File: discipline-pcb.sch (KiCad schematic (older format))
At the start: 164 parts, among them J1 AVR-ISP-6, SW1 KEYSW, SW10 KEYSW, SW11 KEYSW, SW12 KEYSW, SW13 KEYSW, SW14 KEYSW, SW15 KEYSW, SW16 KEYSW, SW17 KEYSW, SW18 KEYSW, SW19 KEYSW, SW2 KEYSW, SW20 KEYSW, SW21 KEYSW, SW22 KEYSW, SW23 KEYSW, SW24 KEYSW, SW25 KEYSW, SW26 KEYSW, SW27 KEYSW, SW28 KEYSW, SW29 KEYSW, SW3 KEYSW, SW30 KEYSW, SW31 KEYSW, SW32 KEYSW, SW33 KEYSW, SW34 KEYSW, SW35 KEYSW, SW36 KEYSW, SW37 KEYSW, SW38 KEYSW, SW39 KEYSW, SW4 KEYSW, SW40 KEYSW, SW41 KEYSW, SW42 KEYSW, SW43 KEYSW, SW44 KEYSW, SW45 KEYSW, SW46 KEYSW, SW47 KEYSW, SW48 KEYSW, SW49 KEYSW, SW5 KEYSW, SW50 KEYSW, SW51 KEYSW, SW52 KEYSW, SW53 KEYSW, SW54 KEYSW, SW55 KEYSW, SW56 KEYSW, SW57 KEYSW, SW58 KEYSW, SW59 KEYSW, SW6 KEYSW, SW60 KEYSW, SW61 KEYSW, SW62 KEYSW, SW63 KEYSW, SW64 KEYSW, SW65 KEYSW, SW66 KEYSW, SW67 KEYSW, SW68 KEYSW, SW69 KEYSW, SW7 KEYSW, SW70 KEYSW, SW71 KEYSW, SW72 KEYSW, SW73 KEYSW, SW74 KEYSW, SW8 KEYSW, SW9 KEYSW, U1 ATmega32A-PU, Y1 Crystal

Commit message: hopefully made it ISO compatible
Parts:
- added D75: (no value), cftkb:D_DO-35_SOD27_P5.08mm_Horizontal, symbol Device:D
- added SW75, SWb43: KEYSW, cftkb:SW_Cherry_MX1A_1.00u_PCB-NOSCREEN, symbol discipline-pcb-rescue:KEYSW-keyboard_parts
- added SWb29: KEYSW, MX_Only:MXOnly-ISO-ROTATED-ReversedStabilizers-NoLED, symbol discipline-pcb-rescue:KEYSW-keyboard_parts
- added SWb45: KEYSW, cftkb:SW_Cherry_MX1A_1.25u_PCBNOSCREEN, symbol discipline-pcb-rescue:KEYSW-keyboard_parts
- BOOT1, RESET1: symbol keyboard_parts:SW_PUSH -> discipline-pcb-rescue:SW_PUSH-keyboard_parts
- SW1, SW10, SW11, SW12, SW13, SW14, SW15, SW16, SW17, SW18, SW19, SW2, SW20, SW21, SW22, SW23, SW24, SW25, SW26, SW27, SW28, SW29, SW3, SW30, SW31, SW32, SW33, SW34, SW35, SW36, SW37, SW38, SW39, SW4, SW40, SW41, SW42, SW43, SW44, SW45, SW46, SW47, SW48, SW49, SW5, SW50, SW51, SW52, SW53, SW54, SW55, SW56, SW57, SW58, SW59, SW6, SW60, SW61, SW62, SW63, SW64, SW65, SW66, SW67, SW68, SW69, SW7, SW70, SW71, SW72, SW73, SW74, SW8, SW9: symbol keyboard_parts:KEYSW -> discipline-pcb-rescue:KEYSW-keyboard_parts
- USB1: symbol Type-C:USB_C_GCT_USB4085 -> discipline-pcb-rescue:USB_C_GCT_USB4085-Type-C
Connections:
- wire segments 342 -> 352

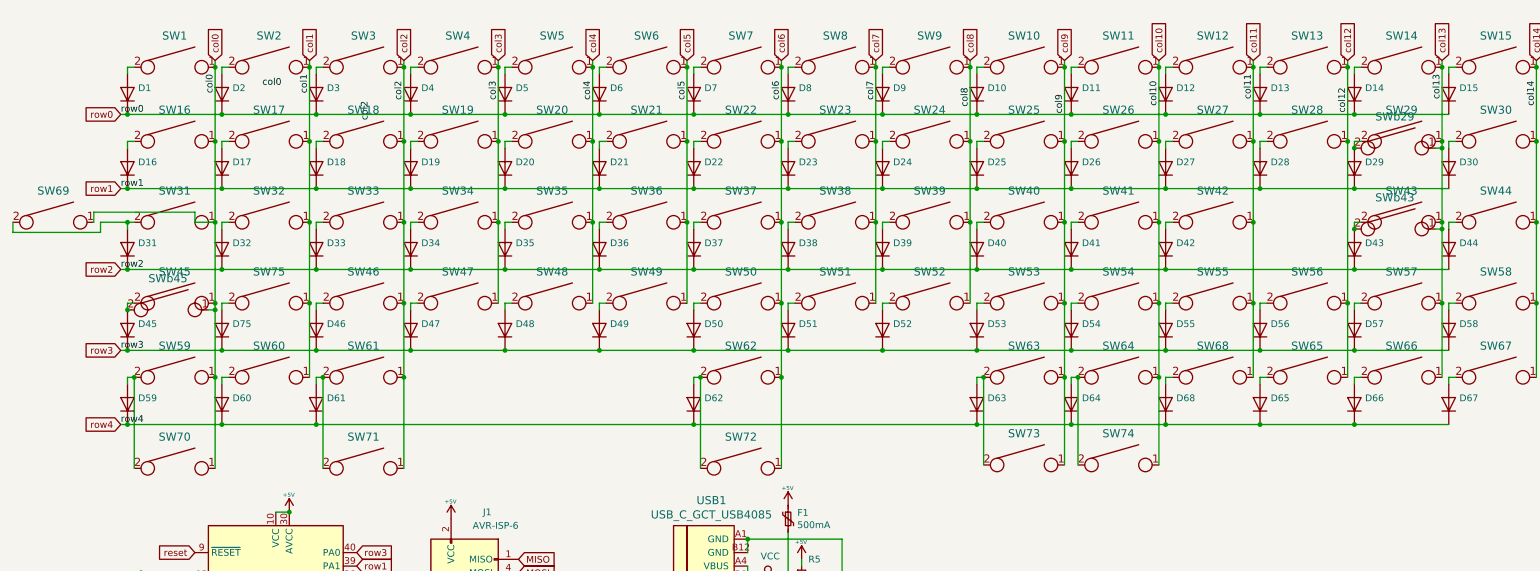
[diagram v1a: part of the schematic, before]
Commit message: fixed some footprints and removed switch options
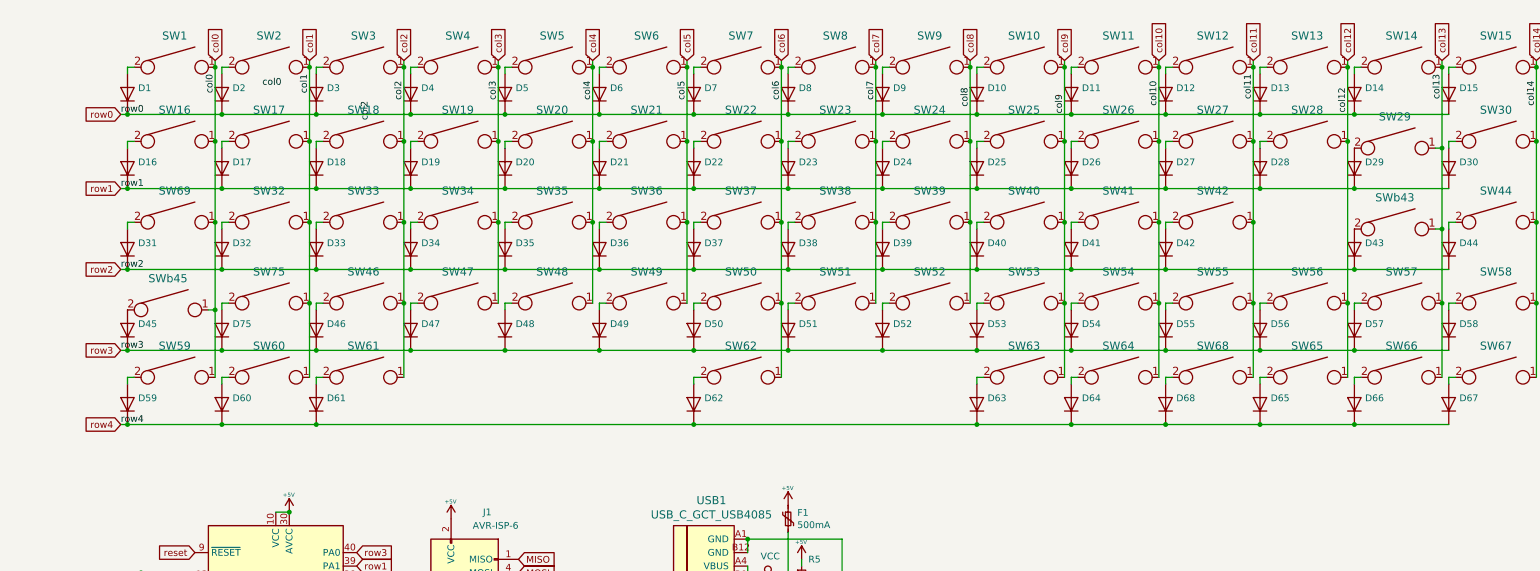
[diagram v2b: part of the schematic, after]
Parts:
- removed SW31: KEYSW, cftkb:SW_Cherry_MX1A_1.75u_PCBNOSCREEN, symbol discipline-pcb-rescue:KEYSW-keyboard_parts
- removed SW43, SW45: KEYSW, cftkb:SW_Cherry_MX1A_2.25u_PCBNOSCREEN, symbol discipline-pcb-rescue:KEYSW-keyboard_parts
- removed SW70, SW71, SW73, SW74: KEYSW, cftkb:SW_Cherry_MX1A_1.50u_PCBNOSCREEN, symbol discipline-pcb-rescue:KEYSW-keyboard_parts
- removed SW72: KEYSW, cftkb:SW_Cherry_MX1A_1.00u_PCB-NOSCREEN, symbol discipline-pcb-rescue:KEYSW-keyboard_parts
- removed SWb29: KEYSW, MX_Only:MXOnly-ISO-ROTATED-ReversedStabilizers-NoLED, symbol discipline-pcb-rescue:KEYSW-keyboard_parts
- C1, C2: footprint cftkb:D_DO-35_SOD27_P5.08mm_Horizontal -> Capacitor_THT:C_Disc_D3.4mm_W2.1mm_P2.50mm
- C3: footprint cftkb:D_DO-35_SOD27_P5.08mm_Horizontal -> Capacitor_THT:CP_Radial_D4.0mm_P1.50mm
- C4, C5: footprint cftkb:D_DO-35_SOD27_P5.08mm_Horizontal -> Capacitor_THT:C_Disc_D5.0mm_W2.5mm_P5.00mm
- SW29: footprint cftkb:SW_Cherry_MX1A_1.50u_PCBNOSCREEN -> cftkb:SW_Cherry_MX1A_2.00u_PCBNOSCREEN
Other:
- moved on the sheet: SW69
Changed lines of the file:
@@
 	11300 3500 11300 3550
-$Comp
-L discipline-pcb-rescue:KEYSW-keyboard_parts SW29
-U 1 1 5BDD4B49
-P 12350 3500
-F 0 "SW29" H 12350 3733 60  0000 C CNN
-F 1 "KEYSW" H 12350 3400 60  0001 C CNN
-F 2 "cftkb:SW_Cherry_MX1A_1.50u_PCBNOSCREEN" H 12350 3500 60  0001 C CNN
-F 3 "" H 12350 3500 60  0000 C CNN
-	1    12350 3500
-	1    0    0    -1
-$EndComp
 $Comp
 L Device:D D29
@@
 	0    -1   -1   0
 $EndComp
-Wire Wire Line
-	12050 3500 12000 3500
-Wire Wire Line
-	12000 3500 12000 3550
 $Comp
 L discipline-pcb-rescue:KEYSW-keyboard_parts SW30
@@
 	12700 3500 12700 3550
 $Comp
-L discipline-pcb-rescue:KEYSW-keyboard_parts SW31
-U 1 1 5BE2E393
-P 3250 4100
-F 0 "SW31" H 3250 4333 60  0000 C CNN
-F 1 "KEYSW" H 3250 4000 60  0001 C CNN
-F 2 "cftkb:SW_Cherry_MX1A_1.75u_PCBNOSCREEN" H 3250 4100 60  0001 C CNN
-F 3 "" H 3250 4100 60  0000 C CNN
-	1    3250 4100
-	1    0    0    -1
-$EndComp
-$Comp
 L Device:D D31
 U 1 1 5BE2E39A
@@
 	0    -1   -1   0
 $EndComp
-Wire Wire Line
-	2950 4100 2900 4100
-Wire Wire Line
-	2900 4100 2900 4150
 $Comp
 L discipline-pcb-rescue:KEYSW-keyboard_parts SW32
@@
 	10600 4100 10600 4150
 $Comp
-L discipline-pcb-rescue:KEYSW-keyboard_parts SW43
-U 1 1 5BE2E453
-P 12350 4100
-F 0 "SW43" H 12350 4333 60  0000 C CNN
-F 1 "KEYSW" H 12350 4000 60  0001 C CNN
-F 2 "cftkb:SW_Cherry_MX1A_2.25u_PCBNOSCREEN" H 12350 4100 60  0001 C CNN
-F 3 "" H 12350 4100 60  0000 C CNN
-	1    12350 4100
-	1    0    0    -1
-$EndComp
-$Comp
 L Device:D D43
 U 1 1 5BE2E45A
@@
 	0    -1   -1   0
 $EndComp
-Wire Wire Line
-	12050 4100 12000 4100
-Wire Wire Line
-	12000 4100 12000 4150
 $Comp
 L discipline-pcb-rescue:KEYSW-keyboard_parts SW44
@@
 	12700 4100 12700 4150
 $Comp
-L discipline-pcb-rescue:KEYSW-keyboard_parts SW45
-U 1 1 5BE34833
-P 3250 4700
-F 0 "SW45" H 3250 4933 60  0000 C CNN
-F 1 "KEYSW" H 3250 4600 60  0001 C CNN
-F 2 "cftkb:SW_Cherry_MX1A_2.25u_PCBNOSCREEN" H 3250 4700 60  0001 C CNN
-F 3 "" H 3250 4700 60  0000 C CNN
-	1    3250 4700
-	1    0    0    -1
-$EndComp
-$Comp
 L Device:D D45
 U 1 1 5BE3483A
@@
 	0    -1   -1   0
 $EndComp
-Wire Wire Line
-	2950 4700 2900 4700
-Wire Wire Line
-	2900 4700 2900 4750
 $Comp
 L discipline-pcb-rescue:KEYSW-keyboard_parts SW46
@@
 F 0 "C2" H 3100 7300 50  0000 L CNN
 F 1 "22p" H 3100 7200 50  0000 L CNN
-F 2 "cftkb:D_DO-35_SOD27_P5.08mm_Horizontal" H 3000 7200 50  0001 C CNN
+F 2 "Capacitor_THT:C_Disc_D3.4mm_W2.1mm_P2.50mm" H 3000 7200 50  0001 C CNN
 F 3 "~" H 3000 7200 50  0001 C CNN
 	1    3000 7200
@@
 F 0 "C1" H 2650 7300 50  0000 L CNN
 F 1 "22p" H 2600 7200 50  0000 L CNN
-F 2 "cftkb:D_DO-35_SOD27_P5.08mm_Horizontal" H 2850 7200 50  0001 C CNN
+F 2 "Capacitor_THT:C_Disc_D3.4mm_W2.1mm_P2.50mm" H 2850 7200 50  0001 C CNN
 F 3 "~" H 2850 7200 50  0001 C CNN
 	1    2850 7200
@@
 F 0 "C3" H 5350 10250 50  0000 L CNN
 F 1 "4.7u" H 5300 9950 50  0000 L CNN
-F 2 "cftkb:D_DO-35_SOD27_P5.08mm_Horizontal" H 5400 10100 50  0001 C CNN
+F 2 "Capacitor_THT:CP_Radial_D4.0mm_P1.50mm" H 5400 10100 50  0001 C CNN
 F 3 "~" H 5400 10100 50  0001 C CNN
 	1    5400 10100
@@
 F 0 "C4" H 5500 10250 50  0000 L CNN
 F 1 "0.1u" H 5500 9950 50  0000 L CNN
-F 2 "cftkb:D_DO-35_SOD27_P5.08mm_Horizontal" H 5550 10100 50  0001 C CNN
+F 2 "Capacitor_THT:C_Disc_D5.0mm_W2.5mm_P5.00mm" H 5550 10100 50  0001 C CNN
 F 3 "~" H 5550 10100 50  0001 C CNN
 	1    5550 10100
@@
 F 0 "C5" H 5650 10250 50  0000 L CNN
 F 1 "0.1u" H 5700 9950 50  0000 L CNN
-F 2 "cftkb:D_DO-35_SOD27_P5.08mm_Horizontal" H 5700 10100 50  0001 C CNN
+F 2 "Capacitor_THT:C_Disc_D5.0mm_W2.5mm_P5.00mm" H 5700 10100 50  0001 C CNN
 F 3 "~" H 5700 10100 50  0001 C CNN
 	1    5700 10100
@@
 Connection ~ 3550 3500
 Wire Wire Line
-	3550 3500 3550 4100
-Connection ~ 3550 4100
-Wire Wire Line
-	3550 4100 3550 4700
-Connection ~ 3550 4700
-Wire Wire Line
-	3550 4700 3550 4750
-Wire Wire Line
 	4250 2900 4250 2950
 Connection ~ 4250 2950
@@
 	12650 2900 12650 2950
 Connection ~ 12650 2950
-Wire Wire Line
-	12650 2950 12650 3500
-Connection ~ 12650 3500
-Wire Wire Line
-	12650 3500 12650 3550
-Connection ~ 12650 4100
-Wire Wire Line
-	12650 4100 12650 4150
 Connection ~ 12650 4700
 Wire Wire Line
@@
 L discipline-pcb-rescue:KEYSW-keyboard_parts SW69
 U 1 1 5DC1DEA4
-P 2350 4100
-F 0 "SW69" H 2350 4333 60  0000 C CNN
-F 1 "KEYSW" H 2350 4000 60  0001 C CNN
-F 2 "cftkb:SW_Cherry_MX1A_1.25u_PCBNOSCREEN" H 2350 4100 60  0001 C CNN
-F 3 "" H 2350 4100 60  0000 C CNN
-	1    2350 4100
-	1    0    0    -1
-$EndComp
-Wire Wire Line
-	2650 4100 2650 4025
-Wire Wire Line
-	2650 4025 3400 4025
-Wire Wire Line
-	3400 4025 3400 4100
-Wire Wire Line
-	3400 4100 3550 4100
-Wire Wire Line
-	2900 4100 2700 4100
-Wire Wire Line
-	2700 4100 2700 4175
-Wire Wire Line
-	2700 4175 2050 4175
-Wire Wire Line
-	2050 4175 2050 4100
-Connection ~ 2900 4100
-$Comp
-L discipline-pcb-rescue:KEYSW-keyboard_parts SW70
-U 1 1 5DC5E2A2
-P 3250 5925
-F 0 "SW70" H 3250 6158 60  0000 C CNN
-F 1 "KEYSW" H 3250 5825 60  0001 C CNN
-F 2 "cftkb:SW_Cherry_MX1A_1.50u_PCBNOSCREEN" H 3250 5925 60  0001 C CNN
-F 3 "" H 3250 5925 60  0000 C CNN
-	1    3250 5925
-	1    0    0    -1
-$EndComp
-Wire Wire Line
-	2950 5925 2950 5250
-Connection ~ 2950 5250
-Wire Wire Line
-	3550 5925 3550 5250
-Connection ~ 3550 5250
-$Comp
-L discipline-pcb-rescue:KEYSW-keyboard_parts SW71
-U 1 1 5DC9EC8E
-P 4650 5925
-F 0 "SW71" H 4650 6158 60  0000 C CNN
-F 1 "KEYSW" H 4650 5825 60  0001 C CNN
-F 2 "cftkb:SW_Cherry_MX1A_1.50u_PCBNOSCREEN" H 4650 5925 60  0001 C CNN
-F 3 "" H 4650 5925 60  0000 C CNN
-	1    4650 5925
-	1    0    0    -1
-$EndComp
-Wire Wire Line
-	4350 5925 4350 5250
-Connection ~ 4350 5250
-Wire Wire Line
-	4950 5925 4950 5250
-Connection ~ 4950 5250
-$Comp
-L discipline-pcb-rescue:KEYSW-keyboard_parts SW72
-U 1 1 5DCE7558
-P 7450 5925
-F 0 "SW72" H 7450 6158 60  0000 C CNN
-F 1 "KEYSW" H 7450 5825 60  0001 C CNN
-F 2 "cftkb:SW_Cherry_MX1A_1.00u_PCB-NOSCREEN" H 7450 5925 60  0001 C CNN
-F 3 "" H 7450 5925 60  0000 C CNN
-	1    7450 5925
-	1    0    0    -1
-$EndComp
-Wire Wire Line
-	7150 5925 7150 5250
-Connection ~ 7150 5250
-Wire Wire Line
-	7750 5925 7750 5250
-Connection ~ 7750 5250
-$Comp
-L discipline-pcb-rescue:KEYSW-keyboard_parts SW73
-U 1 1 5DD3207D
-P 9550 5900
-F 0 "SW73" H 9550 6133 60  0000 C CNN
-F 1 "KEYSW" H 9550 5800 60  0001 C CNN
-F 2 "cftkb:SW_Cherry_MX1A_1.50u_PCBNOSCREEN" H 9550 5900 60  0001 C CNN
-F 3 "" H 9550 5900 60  0000 C CNN
-	1    9550 5900
-	1    0    0    -1
-$EndComp
-Wire Wire Line
-	9250 5900 9250 5250
-Connection ~ 9250 5250
-Wire Wire Line
-	9850 5900 9850 5250
-Connection ~ 9850 5250
-$Comp
-L discipline-pcb-rescue:KEYSW-keyboard_parts SW74
-U 1 1 5DD72960
-P 10250 5900
-F 0 "SW74" H 10250 6133 60  0000 C CNN
-F 1 "KEYSW" H 10250 5800 60  0001 C CNN
-F 2 "cftkb:SW_Cherry_MX1A_1.50u_PCBNOSCREEN" H 10250 5900 60  0001 C CNN
-F 3 "" H 10250 5900 60  0000 C CNN
-	1    10250 5900
-	1    0    0    -1
-$EndComp
-Wire Wire Line
-	9950 5900 9950 5250
-Connection ~ 9950 5250
-Wire Wire Line
-	10550 5900 10550 5250
-Connection ~ 10550 5250
+P 3250 4100
+F 0 "SW69" H 3250 4333 60  0000 C CNN
+F 1 "KEYSW" H 3250 4000 60  0001 C CNN
+F 2 "cftkb:SW_Cherry_MX1A_1.25u_PCBNOSCREEN" H 3250 4100 60  0001 C CNN
+F 3 "" H 3250 4100 60  0000 C CNN
+	1    3250 4100
+	1    0    0    -1
+$EndComp
 $Comp
 L MCU_Microchip_ATmega:ATmega32A-PU U1
@@
 $EndComp
 Connection ~ 4100 6250
-$Comp
-L discipline-pcb-rescue:KEYSW-keyboard_parts SWb29
-U 1 1 5DB34BFB
-P 12300 3550
-F 0 "SWb29" H 12300 3783 60  0000 C CNN
-F 1 "KEYSW" H 12300 3450 60  0001 C CNN
-F 2 "MX_Only:MXOnly-ISO-ROTATED-ReversedStabilizers-NoLED" H 12300 3550 60  0001 C CNN
-F 3 "" H 12300 3550 60  0000 C CNN
-	1    12300 3550
-	1    0    0    -1
-$EndComp
-Connection ~ 12000 3550
 Wire Wire Line
 	12600 3550 12650 3550
 Connection ~ 12650 3550
-Wire Wire Line
-	12650 3550 12650 4100
 $Comp
 L discipline-pcb-rescue:KEYSW-keyboard_parts SWb43
@@
 	1    0    0    -1
 $EndComp
-Connection ~ 12000 4150
 Wire Wire Line
 	12600 4150 12650 4150
@@
 	1    0    0    -1
 $EndComp
-Connection ~ 2900 4750
 Wire Wire Line
 	3500 4750 3550 4750
@@
 Wire Wire Line
 	3550 4750 3550 5250
+Wire Wire Line
+	12650 2950 12650 3550
+Wire Wire Line
+	12650 3550 12650 4150
+Wire Wire Line
+	3550 3500 3550 4100
+Connection ~ 3550 4100
+Wire Wire Line
+	2950 4100 2900 4100
+Wire Wire Line
+	2900 4100 2900 4150
+Wire Wire Line
+	3550 4100 3550 4750
+$Comp
+L discipline-pcb-rescue:KEYSW-keyboard_parts SW29
+U 1 1 5DE00CA1
+P 12300 3550
+F 0 "SW29" H 12300 3783 60  0000 C CNN
+F 1 "KEYSW" H 12300 3450 60  0001 C CNN
+F 2 "cftkb:SW_Cherry_MX1A_2.00u_PCBNOSCREEN" H 12300 3550 60  0001 C CNN
+F 3 "" H 12300 3550 60  0000 C CNN
+	1    12300 3550
+	1    0    0    -1
+$EndComp
 $EndSCHEMATC
